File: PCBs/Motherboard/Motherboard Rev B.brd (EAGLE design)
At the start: 160 x 100 mm, 38 parts, among them Q1 32kHZ, U1 Value

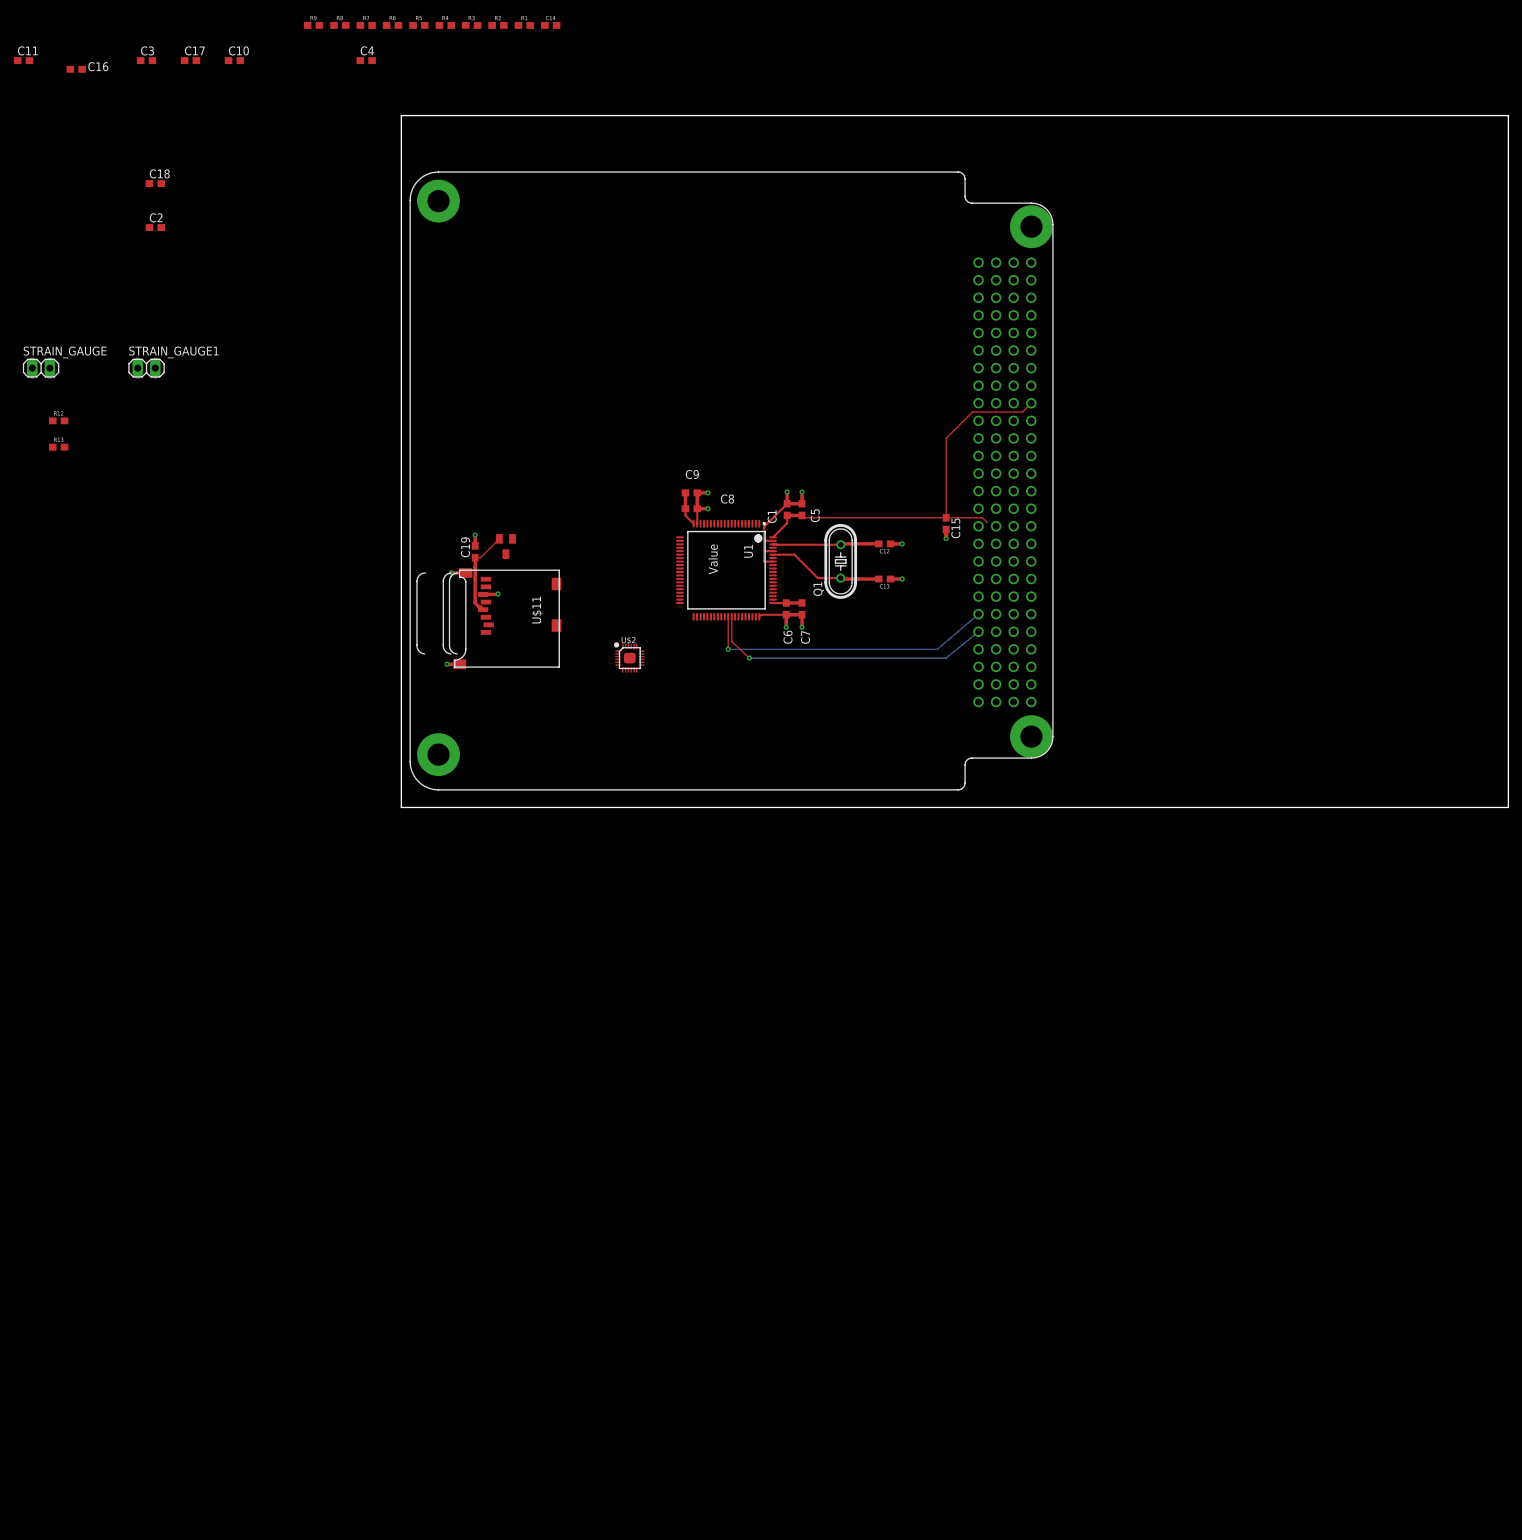
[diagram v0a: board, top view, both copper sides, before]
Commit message: First working draft... still missing sensing and JTAG elements
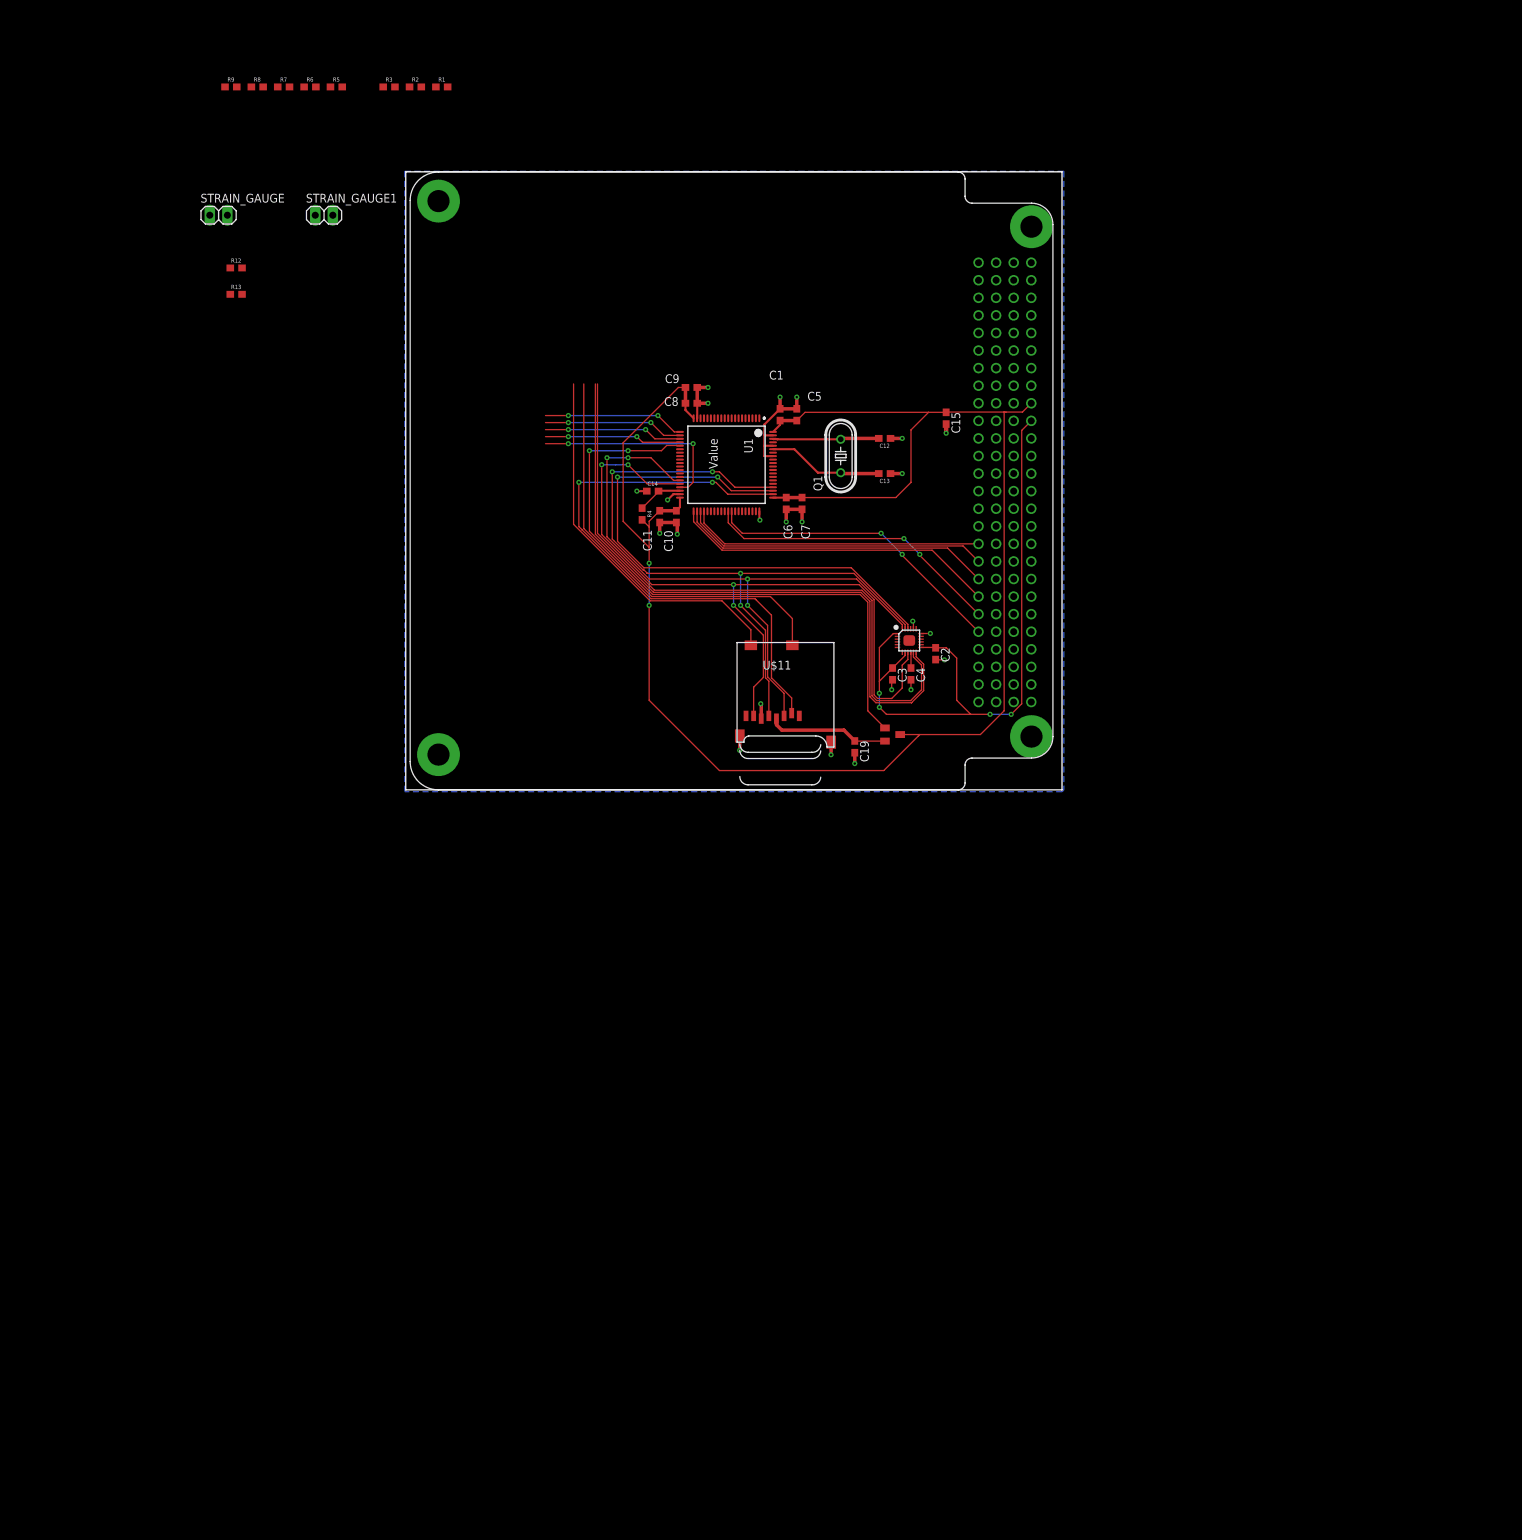
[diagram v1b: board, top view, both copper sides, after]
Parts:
- removed C16: 10uF, adafruit:C0603
- removed C17, C18: 0.1uF, adafruit:C0603
- moved C3 139.6 mm to (71.0, 19.3), turned to 270 degrees
- moved C2 128.5 mm to (77.2, 22.2), turned to 270 degrees
- moved C4 118.6 mm to (73.7, 19.3), turned to 270 degrees
- moved C11 113.1 mm to (37.3, 42.0), turned to 270 degrees
- moved C10 91.8 mm to (39.8, 42.0), turned to 270 degrees
- moved R4 76.1 mm to (34.8, 42.4), turned to 270 degrees
- moved C14 68.9 mm to (36.3, 45.7)
- moved U$3 62.1 mm to (71.0, 10.5), turned to 270 degrees
- moved C19 61.7 mm to (65.5, 8.76), turned to 270 degrees
- moved U$2 40.5 mm to (73.4, 24.1)
- moved R13 33.9 mm to (-23.9, 74.2)
- moved STRAIN_GAUGE 33.9 mm to (-26.4, 85.6)
- moved R12 33.9 mm to (-23.9, 78.0)
- moved STRAIN_GAUGE1 33.9 mm to (-11.2, 85.6)
- moved U$11 27.7 mm to (48.5, 23.9), turned to 0 degrees
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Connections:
- removed net SW5: C16.1, C17.1, U$1.P$65
- new net CARD_DET1: U$11.CD1
- new net CARD_DET2: U$11.CD2
- new net JTAG_CLK: U1.24
- new net JTAG_DI: U1.22
- new net JTAG_DO: U1.21
- new net JTAG_ENABLE: U1.37
- new net JTAG_STATE: U1.23
- net AGND: no longer U$1.P$73
- net GND: now also U$1.P$73; no longer C16.2, C17.2, C18.2
- net LITHIUM_RX: now also U1.42
- net LITHIUM_TX: now also U1.41
- net MISO: now also U$2.9; no longer U$2.24
- net MOSI: now also U$2.24; no longer U$2.9
- net PINAVL1_RX: now also U1.43; no longer U1.41
- net PINAVL1_TX: now also U1.44; no longer U1.42
- net SD_ENABLE: now also U1.25; no longer U1.34
- net SS_SD: now also U1.62
- net SW10: no longer C18.1
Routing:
- net SW8: track 68.4 -> 244.9 mm, vias 0 -> 2
- net MISO: track 0.00 -> 111.3 mm, vias 0 -> 4
- net SCLK: track 0.00 -> 104.4 mm, vias 0 -> 4
- net SW10: track 0.00 -> 95.7 mm, vias 0 -> 4
- net INT: track 0.00 -> 94.1 mm
- net MOSI: track 0.00 -> 93.8 mm, vias 0 -> 4
- net FSYNC: track 0.00 -> 93.1 mm
- net SD_ENABLE: track 0.00 -> 88.7 mm, vias 0 -> 2
- net SS_SD: track 0.00 -> 83.8 mm, vias 0 -> 2
- net SS_IMU: track 0.00 -> 80.2 mm, vias 0 -> 2
- net CARD_DET2: track 0.00 -> 60.3 mm
- net CARD_DET1: track 0.00 -> 54.5 mm
- net LITHIUM_TX: track 0.00 -> 47.2 mm
- net LITHIUM_RX: track 0.00 -> 45.7 mm
- net PINAVL1_RX: track 0.00 -> 44.1 mm
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- added copper zone on layer 16, net GND
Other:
- board size 160 x 100 mm -> 94.8 x 89.3 mm
- board text added: "JTAG"
- board text added: "Potentially useful, unused pins"
- board text added: "Split groundplane here for temperature and strain gauge measurements?"

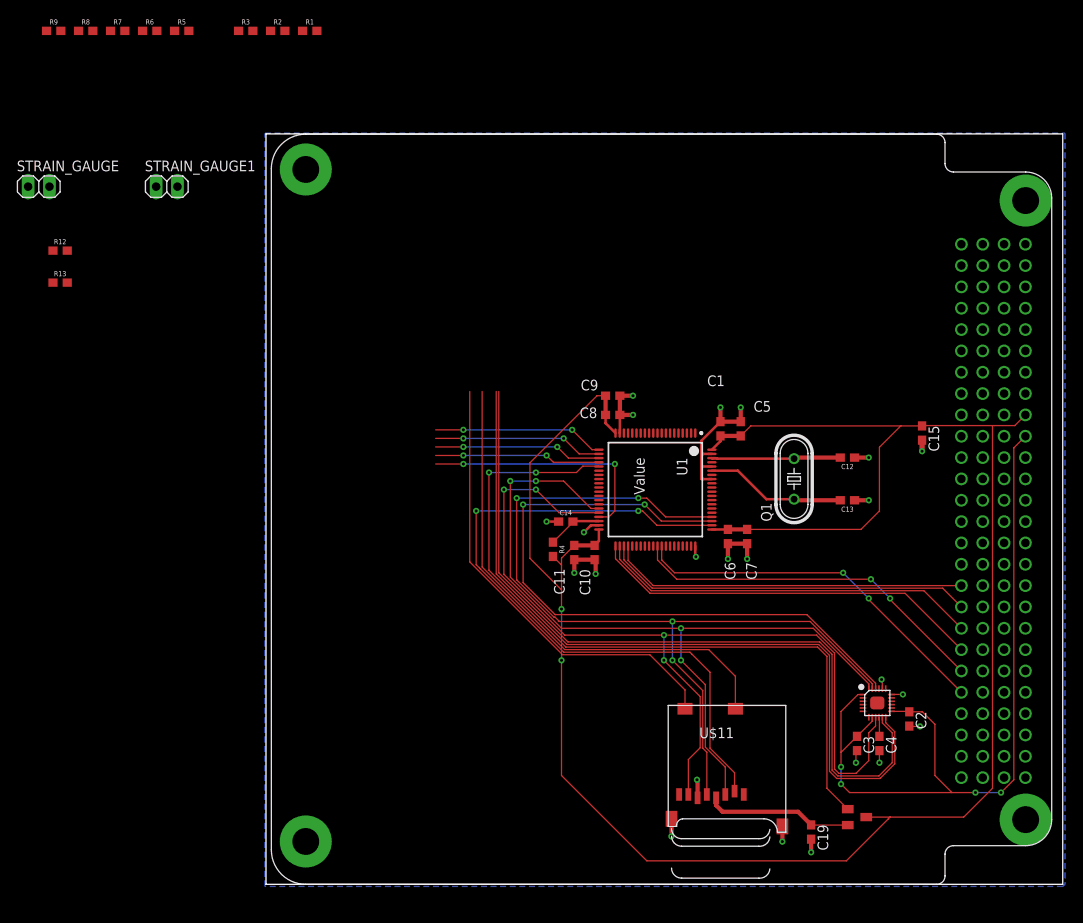
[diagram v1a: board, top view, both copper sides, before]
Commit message: Replace motherboard footprint with new library
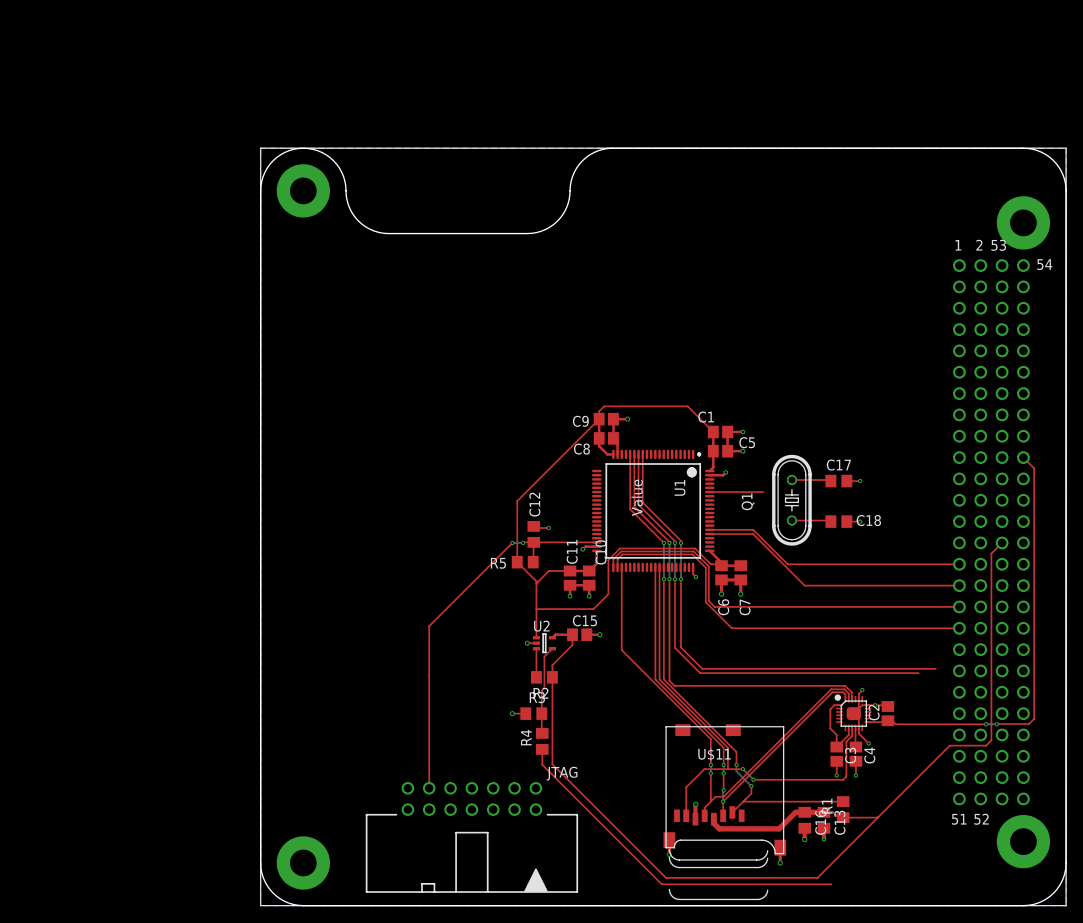
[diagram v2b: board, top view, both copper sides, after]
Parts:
- removed C14: 2.2nF, SparkFun-Capacitors:0603
- removed C19: 10uF, adafruit:C0603
- removed R12: RCAL, SparkFun-Resistors:0603
- removed R13, R6: 950, SparkFun-Resistors:0603
- removed R7, R8, R9: 350, SparkFun-Resistors:0603
- removed STRAIN_GAUGE, STRAIN_GAUGE1: (no value), pinhead:1X02
- removed U$3: FDN340P, FDN340P:SOT23
- added C16: 0.1uF, resistor:C0805
- added C17, C18: 10pF, resistor:C0805
- added JTAG: 2514-5, con-3m:PAK100/2500-5-14
- added U2: TPS22942DCKR, TPS22942:DCK0005A
- C1, C10, C11, C2, C3, C4, C5, C6, C7, C8, C9: device adafruit:C0603 -> adafruit:C0805
- C12: value 10pF -> 2.2nF; device SparkFun-Capacitors:0603 -> resistor:C0805
- C13: value 10pF -> 10uF; device SparkFun-Capacitors:0603 -> resistor:C0805
- C15: value 47uF -> 10uF; device adafruit:C0603 -> adafruit:C0805
- R1: value 350 -> 47k; device SparkFun-Resistors:0603 -> resistor:R0805
- R2, R3: value 350 -> 100k; device SparkFun-Resistors:0603 -> resistor:R0805
- R4: value 47K -> 0; device SparkFun-Resistors:0603 -> resistor:R0805
- R5: value RCAL -> 47k; device SparkFun-Resistors:0603 -> resistor:R0805
- U$1: value PC104 -> PC104_MOBO; device Cubesat:PC104 -> Cubesat:PC104_MOBO
- moved R1 112.4 mm to (69.3, 11.4), turned to 90 degrees
- moved R3 88.2 mm to (32.5, 22.9)
- moved R2 83.3 mm to (33.8, 27.2), turned to 180 degrees
- moved R5 75.3 mm to (31.5, 40.9), turned to 180 degrees
- moved C15 47.3 mm to (38.0, 32.3), turned to 0 degrees
- moved C12 38.4 mm to (32.5, 44.2), turned to 90 degrees
- moved C13 38.2 mm to (67.1, 10.2), turned to 270 degrees
- moved R4 22.9 mm to (33.5, 19.6), turned to 90 degrees
- moved C6 4.38 mm to (54.9, 39.6)
- moved C7 4.38 mm to (57.1, 39.6)
- moved C5 3.60 mm to (54.7, 54.1), turned to 0 degrees
- moved C10 3.11 mm to (39.1, 39.0)
- moved C11 3.09 mm to (36.8, 39.0)
- moved U$2 3.07 mm to (70.6, 22.9)
- moved C4 3.07 mm to (70.9, 18.0)
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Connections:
- removed net ADC1: R3.1, STRAIN_GAUGE.1, U1.1
- removed net ADC2: U1.2
- removed net ADC3: R9.1, STRAIN_GAUGE1.1, U1.3
- removed net ADC4: U1.16
- removed net CARD_DET1: U$11.CD1
- removed net CARD_DET2: U$11.CD2
- removed net FSYNC: U$2.11
- removed net JTAG_CLK: U1.24
- removed net JTAG_DI: U1.22
- removed net JTAG_DO: U1.21
- removed net JTAG_ENABLE: U1.37
- removed net JTAG_STATE: U1.23
- removed net N$6: R7.1, R8.2
- removed net N$7: C14.2, R4.1, U1.38
- removed net N$9: R5.1, R6.2
- removed net SD_ENABLE: U$3.1, U1.25
- removed net SS_IMU: U$2.22, U1.63
- removed net SS_SD: U$11.2, U1.62
- removed net SW8: C1.1, C10.1, C11.1, C15.1, C5.1, C6.1, C7.1, C8.1, C9.1, R4.2, U$1.P$70, U$3.3, U1.20, U1.40, U1.61, U1.80
- removed net TEMP1: R5.2, U$1.P$1
- removed net TEMP2: R12.2, U$1.P$3
- removed net VDD: C19.1, U$11.4, U$3.2
- new net 3V3: C13.1, C15.1, C16.1, R1.1, R2.1, U$1.79, U$11.4, U2.5
- new net 3V3_UC: C1.1, C10.1, C11.1, C5.1, C6.1, C7.1, C8.1, C9.1, R5.2, U1.20, U1.40, U1.61, U1.80, U2.1
- new net CS_IMU: U$2.22, U1.15
- new net CS_SD: R1.2, U$11.2, U1.16
- new net DNU_TEMP_ADC: U1.4
- new net LI_OA_RESET: R4.1, U$1.47
- new net RST: C12.1, JTAG.11, R5.1, U1.38
- new net TCK: JTAG.7, U1.24
- new net TDI: JTAG.3, U1.22
- new net TDO: JTAG.1, U1.21
- new net TEST: JTAG.8, U1.37
- new net TMS: JTAG.5, U1.23
- net AGND: now also U$1.61, U$1.66, U$1.69, U$1.74; no longer R13.1, R2.1, R6.1, R8.1, STRAIN_GAUGE.2, STRAIN_GAUGE1.2, U$1.P$61, U$1.P$66, U$1.P$69, U$1.P$74
- net GND: now also C12.2, C13.2, C16.2, C17.2, C18.2, JTAG.9, R3.1, U$1.100, U$1.73, U$1.81, U$1.82, U$1.84, U$1.99, U$2.11, U2.2; no longer C12.1, C13.1, C14.1, C19.2, U$1.P$73, U$1.P$81, U$1.P$82, U$1.P$84
- net LITHIUM_RX: now also U$1.29, U1.66; no longer U$1.P$37, U1.42
- net LITHIUM_TX: now also U$1.31, U1.65; no longer U$1.P$39, U1.41
- net MISO: now also U1.52; no longer U1.36
- net MOSI: now also U1.51; no longer U1.35
- net N$1: now also R2.2, U2.3; no longer C12.2, Q1.2, U1.78
- net N$2: now also C17.1, Q1.2, U1.78; no longer R1.1, R2.2
- net N$4: now also C18.1, Q1.1, U1.75; no longer R12.1, R13.2
- net N$5: now also R3.2, R4.2, U2.4; no longer C13.2, Q1.1, U1.75
- net PINAVL1_RX: now also U$1.35, U1.42; no longer U$1.P$35, U1.43
- net PINAVL1_TX: now also U$1.33, U1.41; no longer U$1.P$33, U1.44
- net SCL: now also U$1.43, U1.14; no longer U$1.P$43, U1.52
- net SCLK: now also U1.43; no longer U1.64
- net SDA: now also U$1.41, U1.13; no longer U$1.P$41, U1.51
- net SW10: now also U$1.72; no longer R1.2, R3.2, R7.2, R9.2, U$1.P$72
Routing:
- net SW8: track 244.9 -> 0.00 mm, vias 2 -> 0
- net 3V3: track 0.00 -> 129.2 mm
- net 3V3_UC: track 0.00 -> 99.7 mm
- net INT: track 94.1 -> 0.00 mm
- net FSYNC: track 93.1 -> 0.00 mm
- net SD_ENABLE: track 88.7 -> 0.00 mm, vias 2 -> 0
- net SS_SD: track 83.8 -> 0.00 mm, vias 2 -> 0
- net SS_IMU: track 80.2 -> 0.00 mm, vias 2 -> 0
- net CS_SD: track 0.00 -> 61.4 mm, vias 0 -> 4
- net CARD_DET2: track 60.3 -> 0.00 mm
- net CARD_DET1: track 54.5 -> 0.00 mm
- net MISO: track 111.3 -> 57.5 mm, vias 4 -> 2
- net CS_IMU: track 0.00 -> 51.8 mm, vias 0 -> 2
- net SCLK: track 104.4 -> 57.1 mm, vias 4 -> 2
- net RST: track 0.00 -> 45.7 mm, vias 0 -> 2
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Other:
- board size 94.8 x 89.3 mm -> 95.9 x 90.2 mm
- board text removed: "JTAG"
- board text removed: "Potentially useful, unused pins"
- board text removed: "Split groundplane here for temperature and strain gauge measurements?"
